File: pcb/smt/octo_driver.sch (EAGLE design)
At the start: 19 parts, among them U1 LP2985-10DBVT

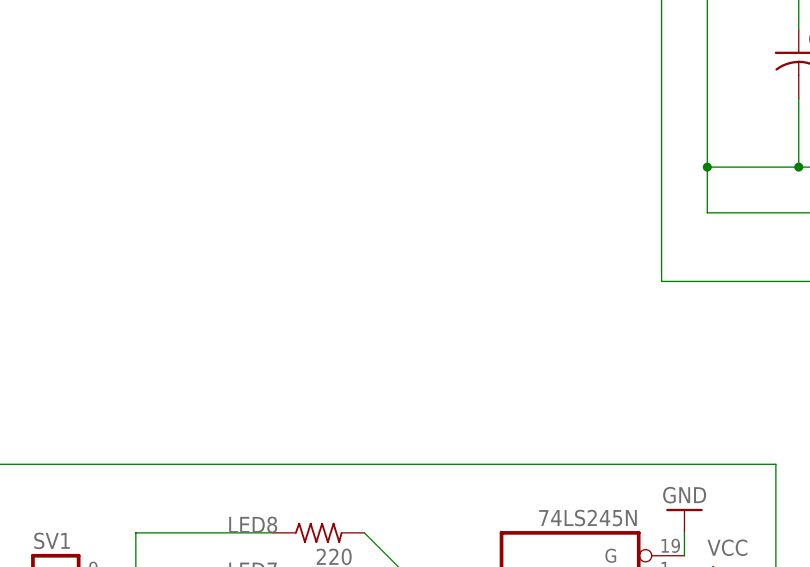
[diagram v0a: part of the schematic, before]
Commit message: added test point
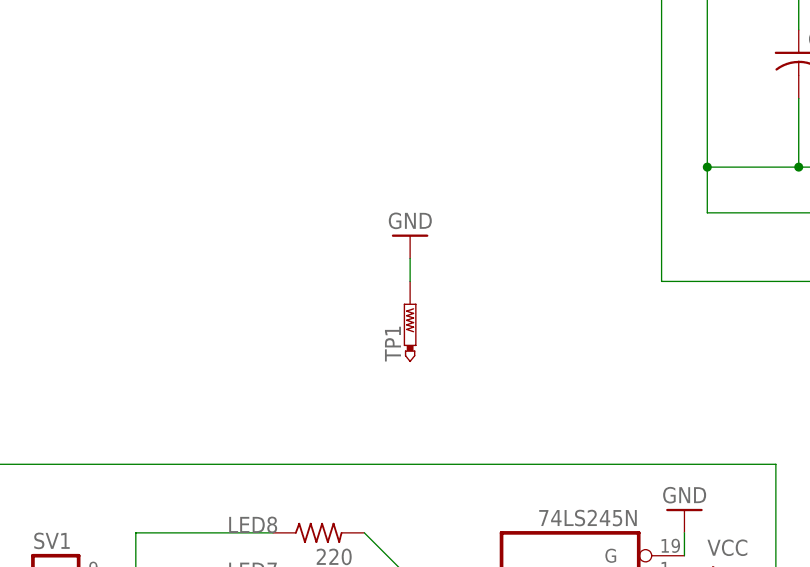
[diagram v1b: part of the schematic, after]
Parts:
- added TP1: PTR1B2,54, testpad:PTR1B2,54
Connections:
- net GND: now also TP1.TP
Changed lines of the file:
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@@
 <part name="P+3" library="supply1" deviceset="VCC" device=""/>
 <part name="P+4" library="supply1" deviceset="VCC" device=""/>
+<part name="TP1" library="testpad" deviceset="PTR1" device="B2,54"/>
+<part name="GND5" library="supply1" deviceset="GND" device=""/>
 </parts>
 <sheets>
@@
 <instance part="P+3" gate="VCC" x="5.08" y="5.08"/>
 <instance part="P+4" gate="VCC" x="50.8" y="43.18" rot="R270"/>
+<instance part="TP1" gate="G$1" x="15.24" y="73.66"/>
+<instance part="GND5" gate="1" x="15.24" y="81.28" rot="R180"/>
 </instances>
 <busses>
@@
 <wire x1="106.68" y1="78.74" x2="106.68" y2="73.66" width="0.1524" layer="91"/>
 </segment>
+<segment>
+<pinref part="TP1" gate="G$1" pin="TP"/>
+<pinref part="GND5" gate="1" pin="GND"/>
+<wire x1="15.24" y1="76.2" x2="15.24" y2="78.74" width="0.1524" layer="91"/>
+</segment>
 </net>
